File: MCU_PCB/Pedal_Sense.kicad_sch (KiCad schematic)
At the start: 12 parts, among them U17 LM4040CELT-3.0, U19 LM4040CELT-3.0, U20 LM4040CELT-3.0

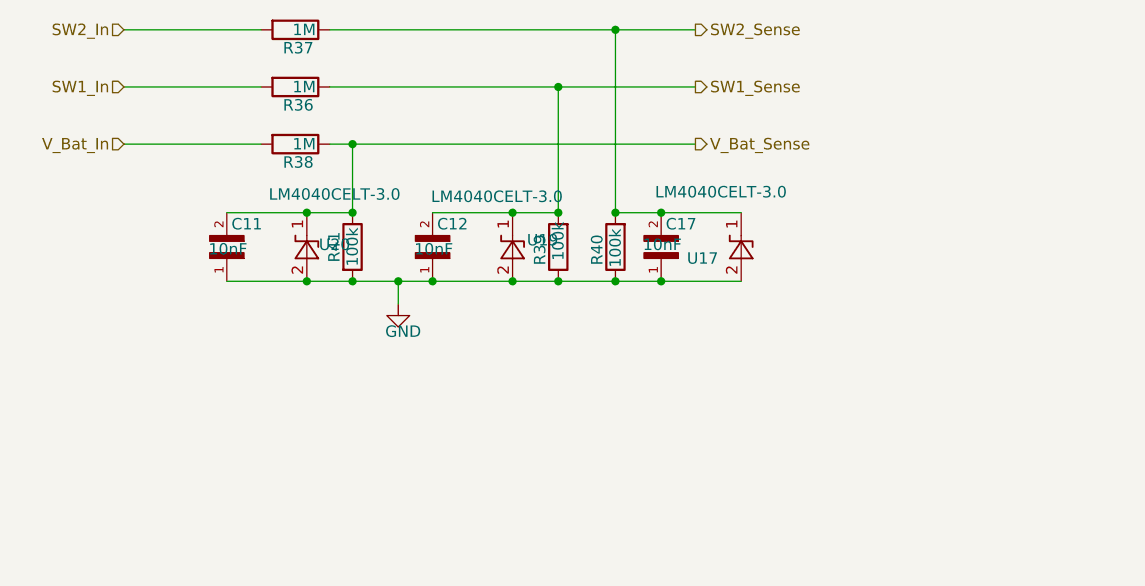
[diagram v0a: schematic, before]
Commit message: sry forgot to push, waiting on PCB shipping atm. Notes: split power distribution into two boards, one for the main 25V distribution, and another for 12V stuff. Also updated CAN transciever. the previous one was a 5V logic one (same logic as its power), and would have fried our ESPs data pins
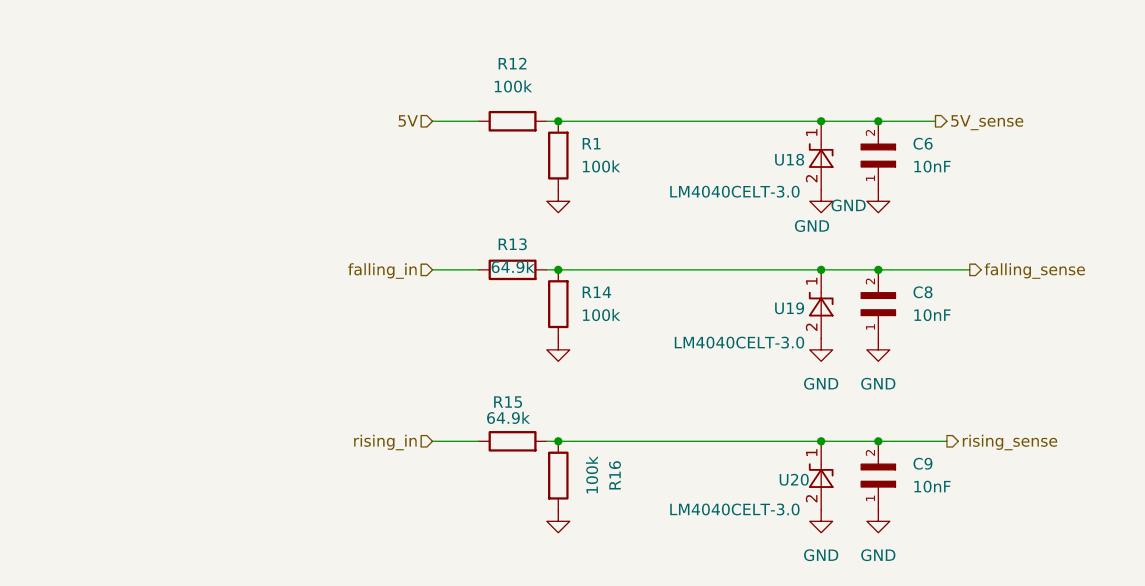
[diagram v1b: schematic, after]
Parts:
- removed C11, C12, C17: 10nF, Capacitor_SMD:C_0805_2012Metric_Pad1.18x1.45mm_HandSolder, symbol C0805C122J5GACTU:C0805C122J5GACTU
- removed R36, R37, R38: 1M, Resistor_SMD:R_0805_2012Metric_Pad1.20x1.40mm_HandSolder, symbol Device:R
- removed R39, R40, R41: 100k, Resistor_SMD:R_0805_2012Metric_Pad1.20x1.40mm_HandSolder, symbol Device:R
- removed U17: LM4040CELT-3.0, Package_TO_SOT_SMD:SOT-23, symbol Reference_Voltage:LM4040DBZ-3
- added C6, C8, C9: 10nF, Capacitor_SMD:C_0805_2012Metric_Pad1.18x1.45mm_HandSolder, symbol C0805C122J5GACTU:C0805C122J5GACTU
- added R1, R12, R14, R16: 100k, Resistor_SMD:R_0805_2012Metric_Pad1.20x1.40mm_HandSolder, symbol Device:R
- added R13, R15: 64.9k, Resistor_SMD:R_0805_2012Metric_Pad1.20x1.40mm_HandSolder, symbol Device:R
- added U18: LM4040CELT-3.0, Package_TO_SOT_SMD:SOT-23, symbol Reference_Voltage:LM4040DBZ-3
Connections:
- net GND: now also C6.1, C8.1, C9.1, R1.1, R14.1, R16.2, U18.2 (A)
- net SW1_Sense renamed falling_sense
- net falling_sense: now also C8.2, R13.2, R14.2
- net V_Bat_Sense renamed rising_sense
- net rising_sense: now also C9.2, R15.2, R16.1
- new net 5V: R12.1
- new net 5V_sense: C6.2, R1.2, R12.2, U18.1 (K)
- new net falling_in: R13.1
- new net rising_in: R15.1
